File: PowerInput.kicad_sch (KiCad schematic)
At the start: 16 parts, among them J17 V_{IN}, Q1 Q_PMOS_GSD, Q2 Q_PMOS_GSD

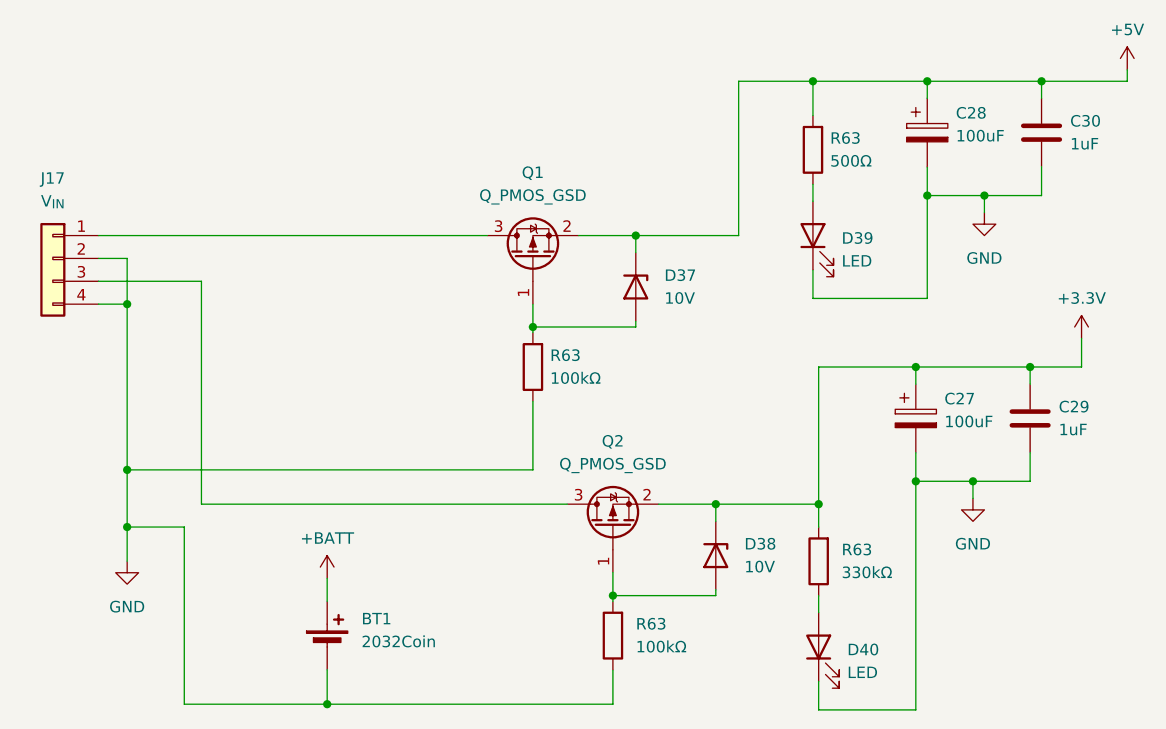
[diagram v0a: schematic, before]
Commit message: Change from TeensyIrrigation to PicoIrrigation and change the connectors. Will use breakout board for I2C MUX if necessary.
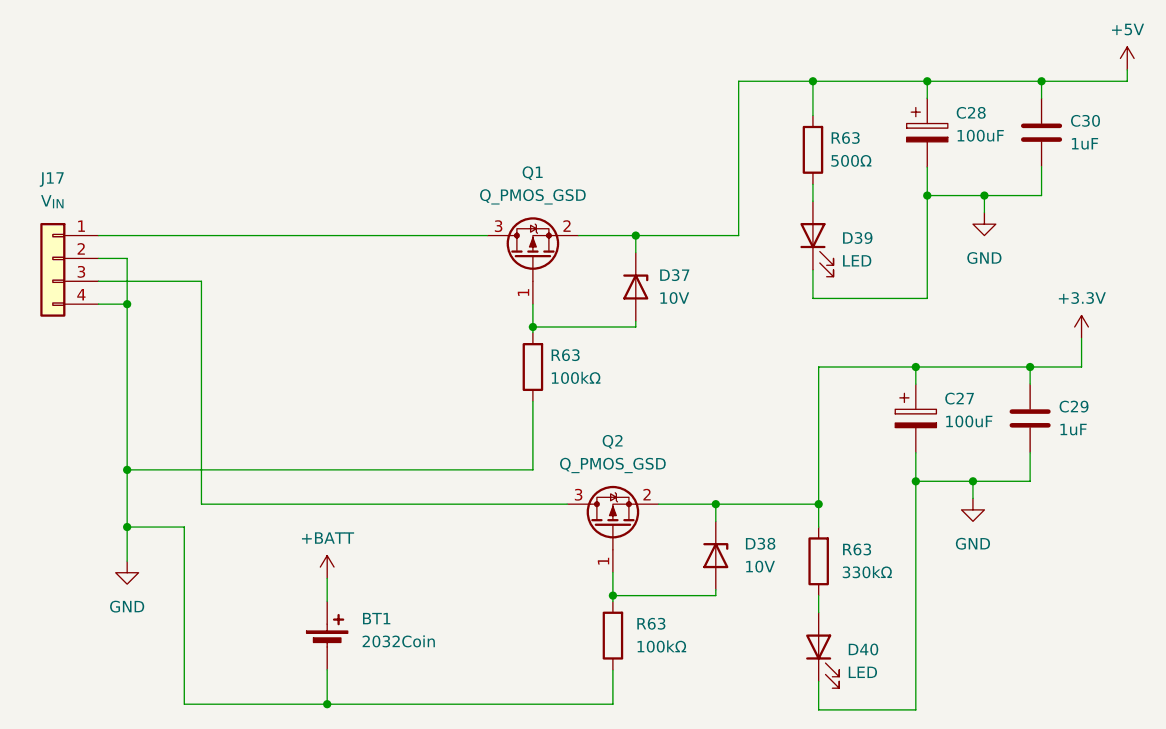
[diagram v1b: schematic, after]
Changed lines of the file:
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@@
     (pin "2")
     (instances
-      (project "TeensyIrrigation"
+      (project "PicoIrrigation"
         (path "/c65a281d-6732-4d62-97b7-333427e1d7dc/b48fcfa8-4ed4-4ed2-b40e-520cd5d82d6e"
           (reference "C30") (unit 1)
@@
     (pin "2")
     (instances
-      (project "TeensyIrrigation"
+      (project "PicoIrrigation"
         (path "/c65a281d-6732-4d62-97b7-333427e1d7dc"
           (reference "R63") (unit 1)
@@
     (pin "2")
     (instances
-      (project "TeensyIrrigation"
+      (project "PicoIrrigation"
         (path "/c65a281d-6732-4d62-97b7-333427e1d7dc/b48fcfa8-4ed4-4ed2-b40e-520cd5d82d6e"
           (reference "D40") (unit 1)
@@
     (pin "2")
     (instances
-      (project "TeensyIrrigation"
+      (project "PicoIrrigation"
         (path "/c65a281d-6732-4d62-97b7-333427e1d7dc/b48fcfa8-4ed4-4ed2-b40e-520cd5d82d6e"
           (reference "D38") (unit 1)
@@
     (pin "2")
     (instances
-      (project "TeensyIrrigation"
+      (project "PicoIrrigation"
         (path "/c65a281d-6732-4d62-97b7-333427e1d7dc/b48fcfa8-4ed4-4ed2-b40e-520cd5d82d6e"
           (reference "C28") (unit 1)
@@
     (pin "1")
     (instances
-      (project "TeensyIrrigation"
+      (project "PicoIrrigation"
         (path "/c65a281d-6732-4d62-97b7-333427e1d7dc/b48fcfa8-4ed4-4ed2-b40e-520cd5d82d6e"
           (reference "#PWR0137") (unit 1)
@@
     (pin "1")
     (instances
-      (project "TeensyIrrigation"
+      (project "PicoIrrigation"
         (path "/c65a281d-6732-4d62-97b7-333427e1d7dc/b48fcfa8-4ed4-4ed2-b40e-520cd5d82d6e"
           (reference "#PWR0138") (unit 1)
@@
     (pin "2")
     (instances
-      (project "TeensyIrrigation"
+      (project "PicoIrrigation"
         (path "/c65a281d-6732-4d62-97b7-333427e1d7dc"
           (reference "BT1") (unit 1)
@@
     (pin "2")
     (instances
-      (project "TeensyIrrigation"
+      (project "PicoIrrigation"
         (path "/c65a281d-6732-4d62-97b7-333427e1d7dc"
           (reference "R63") (unit 1)
@@
     (pin "1")
     (instances
-      (project "TeensyIrrigation"
+      (project "PicoIrrigation"
         (path "/c65a281d-6732-4d62-97b7-333427e1d7dc/b48fcfa8-4ed4-4ed2-b40e-520cd5d82d6e"
           (reference "#PWR0139") (unit 1)
@@
     (pin "4")
     (instances
-      (project "TeensyIrrigation"
+      (project "PicoIrrigation"
         (path "/c65a281d-6732-4d62-97b7-333427e1d7dc/b48fcfa8-4ed4-4ed2-b40e-520cd5d82d6e"
           (reference "J17") (unit 1)
@@
     (pin "2")
     (instances
-      (project "TeensyIrrigation"
+      (project "PicoIrrigation"
         (path "/c65a281d-6732-4d62-97b7-333427e1d7dc"
           (reference "R63") (unit 1)
@@
     (pin "2")
     (instances
-      (project "TeensyIrrigation"
+      (project "PicoIrrigation"
         (path "/c65a281d-6732-4d62-97b7-333427e1d7dc"
           (reference "R63") (unit 1)
@@
     (pin "3")
     (instances
-      (project "TeensyIrrigation"
+      (project "PicoIrrigation"
         (path "/c65a281d-6732-4d62-97b7-333427e1d7dc/b48fcfa8-4ed4-4ed2-b40e-520cd5d82d6e"
           (reference "Q1") (unit 1)
@@
     (pin "1")
     (instances
-      (project "TeensyIrrigation"
+      (project "PicoIrrigation"
         (path "/c65a281d-6732-4d62-97b7-333427e1d7dc/b48fcfa8-4ed4-4ed2-b40e-520cd5d82d6e"
           (reference "#PWR0135") (unit 1)
@@
     (pin "3")
     (instances
-      (project "TeensyIrrigation"
+      (project "PicoIrrigation"
         (path "/c65a281d-6732-4d62-97b7-333427e1d7dc/b48fcfa8-4ed4-4ed2-b40e-520cd5d82d6e"
           (reference "Q2") (unit 1)
@@
   (symbol (lib_id "Device:D_Zener") (at 142.24 74.295 270) (unit 1)
     (in_bom yes) (on_board yes) (dnp no) (fields_autoplaced)
-    (property "Reference" "D37" (at 145.415 73.025 90)
-      (effects (font (size 1.27 1.27)) (justify left))
-    )
-    (property "Value" "10V" (at 145.415 75.565 90)
+    (property "Reference" "D37" (at 144.78 73.025 90)
+      (effects (font (size 1.27 1.27)) (justify left))
+    )
+    (property "Value" "10V" (at 144.78 75.565 90)
       (effects (font (size 1.27 1.27)) (justify left))
     )
@@
     (pin "2")
     (instances
-      (project "TeensyIrrigation"
+      (project "PicoIrrigation"
         (path "/c65a281d-6732-4d62-97b7-333427e1d7dc/b48fcfa8-4ed4-4ed2-b40e-520cd5d82d6e"
           (reference "D37") (unit 1)
@@
     (pin "2")
     (instances
-      (project "TeensyIrrigation"
+      (project "PicoIrrigation"
         (path "/c65a281d-6732-4d62-97b7-333427e1d7dc/b48fcfa8-4ed4-4ed2-b40e-520cd5d82d6e"
           (reference "C27") (unit 1)
@@
     (pin "1")
     (instances
-      (project "TeensyIrrigation"
+      (project "PicoIrrigation"
         (path "/c65a281d-6732-4d62-97b7-333427e1d7dc/b48fcfa8-4ed4-4ed2-b40e-520cd5d82d6e"
           (reference "#PWR0134") (unit 1)
@@
     (pin "1")
     (instances
-      (project "TeensyIrrigation"
+      (project "PicoIrrigation"
         (path "/c65a281d-6732-4d62-97b7-333427e1d7dc/b48fcfa8-4ed4-4ed2-b40e-520cd5d82d6e"
           (reference "#PWR0136") (unit 1)
@@
     (pin "2")
     (instances
-      (project "TeensyIrrigation"
+      (project "PicoIrrigation"
         (path "/c65a281d-6732-4d62-97b7-333427e1d7dc/b48fcfa8-4ed4-4ed2-b40e-520cd5d82d6e"
           (reference "C29") (unit 1)
@@
     (pin "2")
     (instances
-      (project "TeensyIrrigation"
+      (project "PicoIrrigation"
         (path "/c65a281d-6732-4d62-97b7-333427e1d7dc/b48fcfa8-4ed4-4ed2-b40e-520cd5d82d6e"
           (reference "D39") (unit 1)

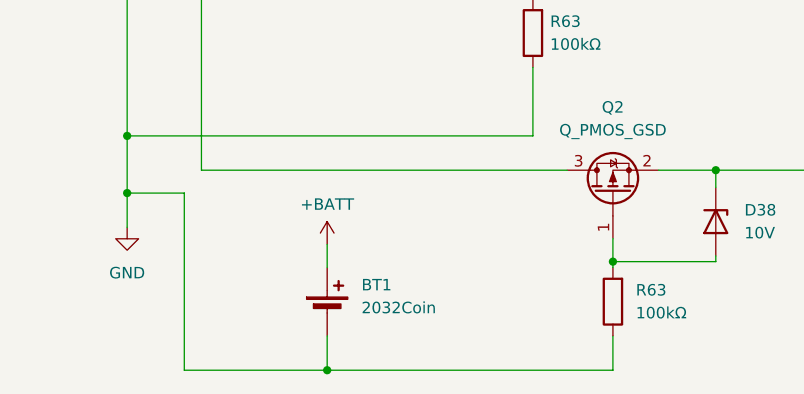
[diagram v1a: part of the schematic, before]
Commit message: Remove battery.
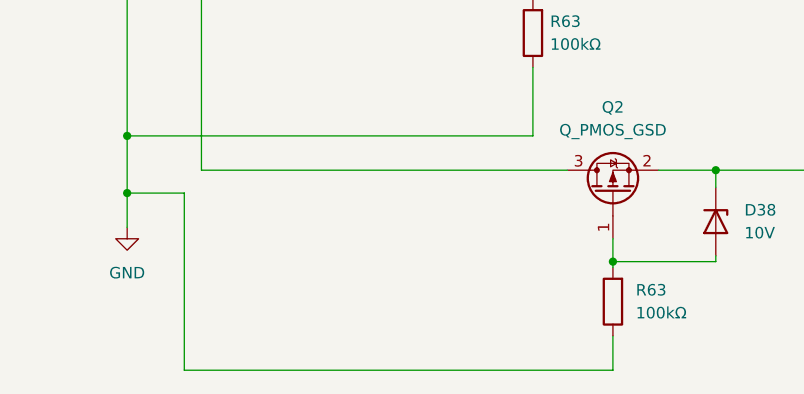
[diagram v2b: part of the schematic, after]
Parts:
- removed BT1: 2032Coin, BatteryCoin:BC2032, symbol Device:Battery_Cell
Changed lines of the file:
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@@
   (junction (at 151.13 98.425) (diameter 0) (color 0 0 0 0)
   )
-  (junction (at 107.95 120.65) (diameter 0) (color 0 0 0 0)
-  )
   (junction (at 142.24 68.58) (diameter 0) (color 0 0 0 0)
   )
@@
     (stroke (width 0) (type default))
   )
-  (wire (pts (xy 107.95 106.68) (xy 107.95 109.22))
-    (stroke (width 0) (type default))
-  )
   (wire (pts (xy 180.975 64.135) (xy 180.975 66.04))
     (stroke (width 0) (type default))
@@
     (stroke (width 0) (type default))
   )
-  (wire (pts (xy 139.7 120.65) (xy 107.95 120.65))
-    (stroke (width 0) (type default))
-  )
   (wire (pts (xy 162.56 118.11) (xy 162.56 121.285))
     (stroke (width 0) (type default))
@@
     (stroke (width 0) (type default))
   )
-  (wire (pts (xy 107.95 116.84) (xy 107.95 120.65))
-    (stroke (width 0) (type default))
-  )
   (wire (pts (xy 162.56 83.185) (xy 173.355 83.185))
     (stroke (width 0) (type default))
@@
     (stroke (width 0) (type default))
   )
-  (wire (pts (xy 107.95 120.65) (xy 92.075 120.65))
+  (wire (pts (xy 92.075 120.65) (xy 139.7 120.65))
     (stroke (width 0) (type default))
   )
@@
     )
   )
-  (symbol (lib_id "Device:Battery_Cell") (at 107.95 114.3 0) (unit 1)
-    (in_bom yes) (on_board yes) (dnp no) (fields_autoplaced)
-    (property "Reference" "BT1" (at 111.76 111.1885 0)
-      (effects (font (size 1.27 1.27)) (justify left))
-    )
-    (property "Value" "2032Coin" (at 111.76 113.7285 0)
-      (effects (font (size 1.27 1.27)) (justify left))
-    )
-    (property "Footprint" "BatteryCoin:BC2032" (at 107.95 112.776 90)
-      (effects (font (size 1.27 1.27)) hide)
-    )
-    (property "Datasheet" "~" (at 107.95 112.776 90)
-      (effects (font (size 1.27 1.27)) hide)
-    )
-    (pin "1")
-    (pin "2")
-    (instances
-      (project "PicoIrrigation"
-        (path "/c65a281d-6732-4d62-97b7-333427e1d7dc"
-          (reference "BT1") (unit 1)
-        )
-        (path "/c65a281d-6732-4d62-97b7-333427e1d7dc/b48fcfa8-4ed4-4ed2-b40e-520cd5d82d6e"
-          (reference "BT1") (unit 1)
-        )
-      )
-    )
-  )
   (symbol (lib_id "Device:R") (at 161.925 59.055 180) (unit 1)
     (in_bom yes) (on_board yes) (dnp no) (fields_autoplaced)
@@
         )
       )
-    )
-  )
-  (symbol (lib_id "power:+BATT") (at 107.95 106.68 0) (unit 1)
-    (in_bom yes) (on_board yes) (dnp no) (fields_autoplaced)
-    (property "Reference" "#PWR0135" (at 107.95 110.49 0)
-      (effects (font (size 1.27 1.27)) hide)
-    )
-    (property "Value" "+BATT" (at 107.95 102.235 0)
-      (effects (font (size 1.27 1.27)))
-    )
-    (property "Footprint" "" (at 107.95 106.68 0)
-      (effects (font (size 1.27 1.27)) hide)
-    )
-    (property "Datasheet" "" (at 107.95 106.68 0)
-      (effects (font (size 1.27 1.27)) hide)
-    )
-    (pin "1")
-    (instances
-      (project "PicoIrrigation"
-        (path "/c65a281d-6732-4d62-97b7-333427e1d7dc/b48fcfa8-4ed4-4ed2-b40e-520cd5d82d6e"
-          (reference "#PWR0135") (unit 1)
-        )
-      )

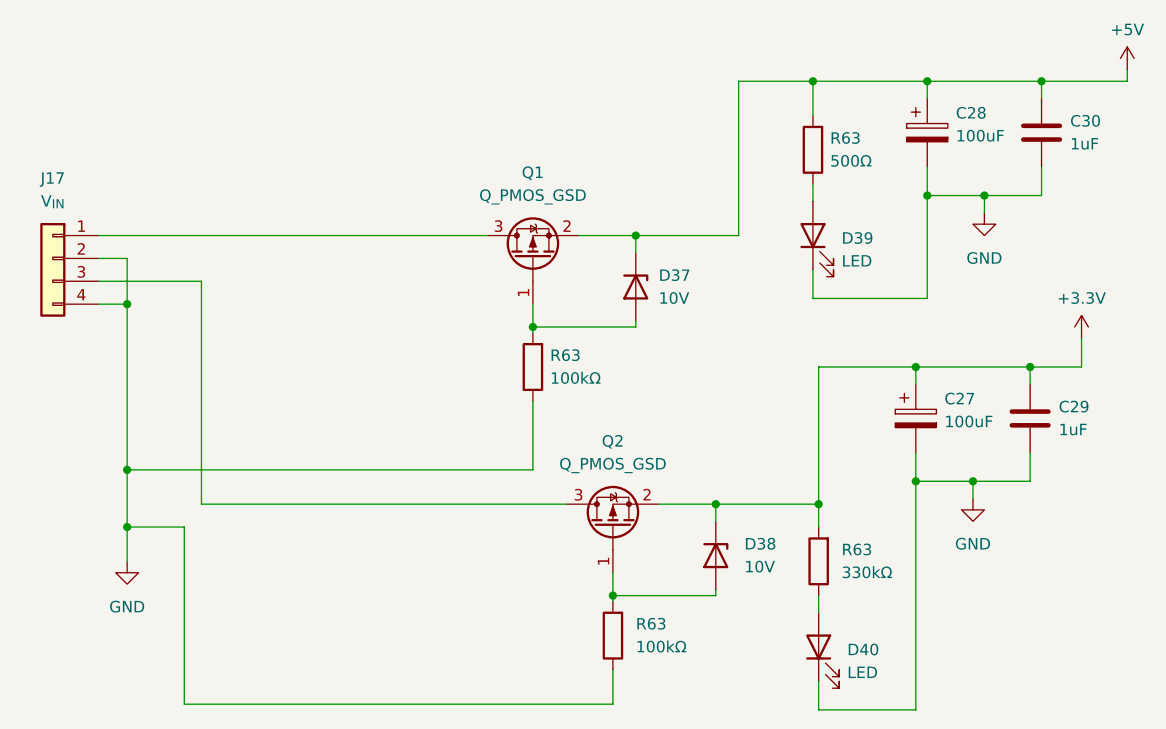
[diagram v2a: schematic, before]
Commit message: Finished schematic. Move to PCB.
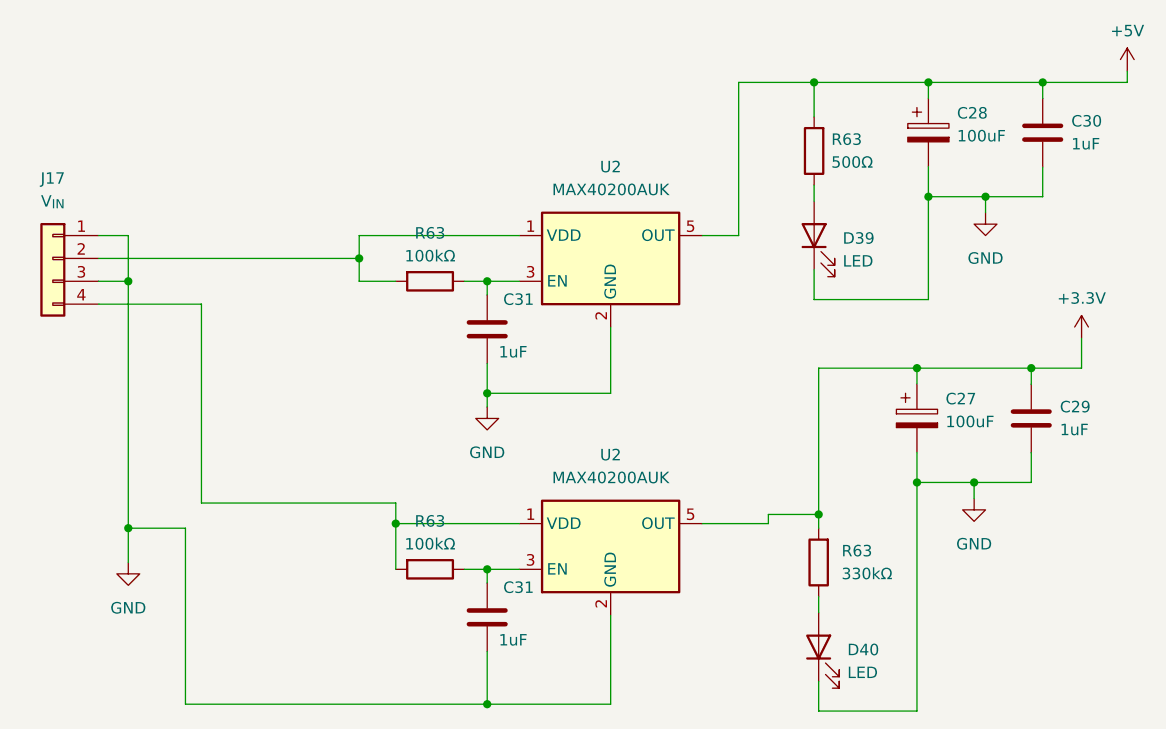
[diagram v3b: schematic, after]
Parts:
- removed D37, D38: 10V, Diode_SMD:D_SOD-123, symbol Device:D_Zener
- removed Q1, Q2: Q_PMOS_GSD, Package_TO_SOT_SMD:SOT-23, symbol Device:Q_PMOS_GSD
- removed R63 (x2): 100kΩ, Resistor_SMD:R_0805_2012Metric, symbol Device:R
- added C31 (x2): 1uF, Capacitor_SMD:C_0805_2012Metric, symbol Device:C
- added R63 (x2): 100kΩ, Resistor_SMD:R_0805_2012Metric, symbol Device:R
- added U2 (x2): MAX40200AUK, Package_TO_SOT_SMD:SOT-23-5, symbol Analog_Switch:MAX40200AUK
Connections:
- net +3.3V: now also U2.5 (OUT)
- net +5V: now also U2.5 (OUT)
- net GND: now also J17.1 (Pin_1), J17.3 (Pin_3), C31.2, C31.2, U2.2 (GND), U2.2 (GND); no longer J17.2 (Pin_2), J17.4 (Pin_4)
- new net: C31.1, R63.1, U2.3 (EN) (x2)
- new net: J17.4 (Pin_4), R63.2, U2.1 (VDD)
- new net: J17.2 (Pin_2), R63.2, U2.1 (VDD)
